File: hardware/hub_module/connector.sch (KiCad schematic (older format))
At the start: 4 parts, among them U2 conn2x18pcie

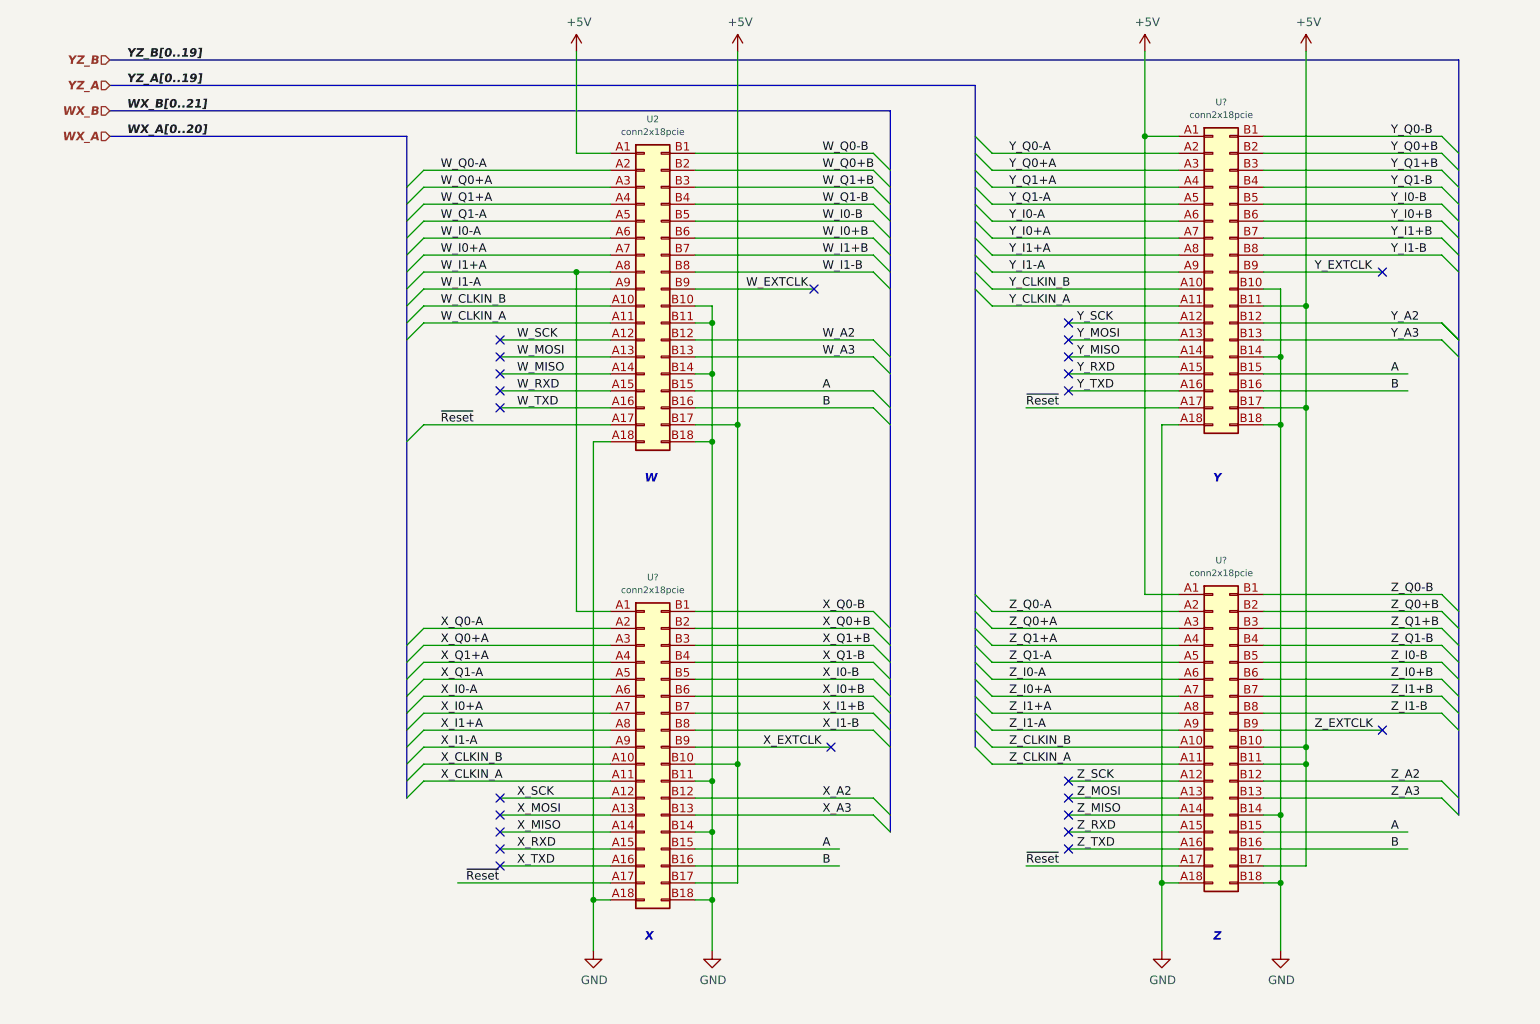
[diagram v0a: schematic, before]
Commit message: busses added
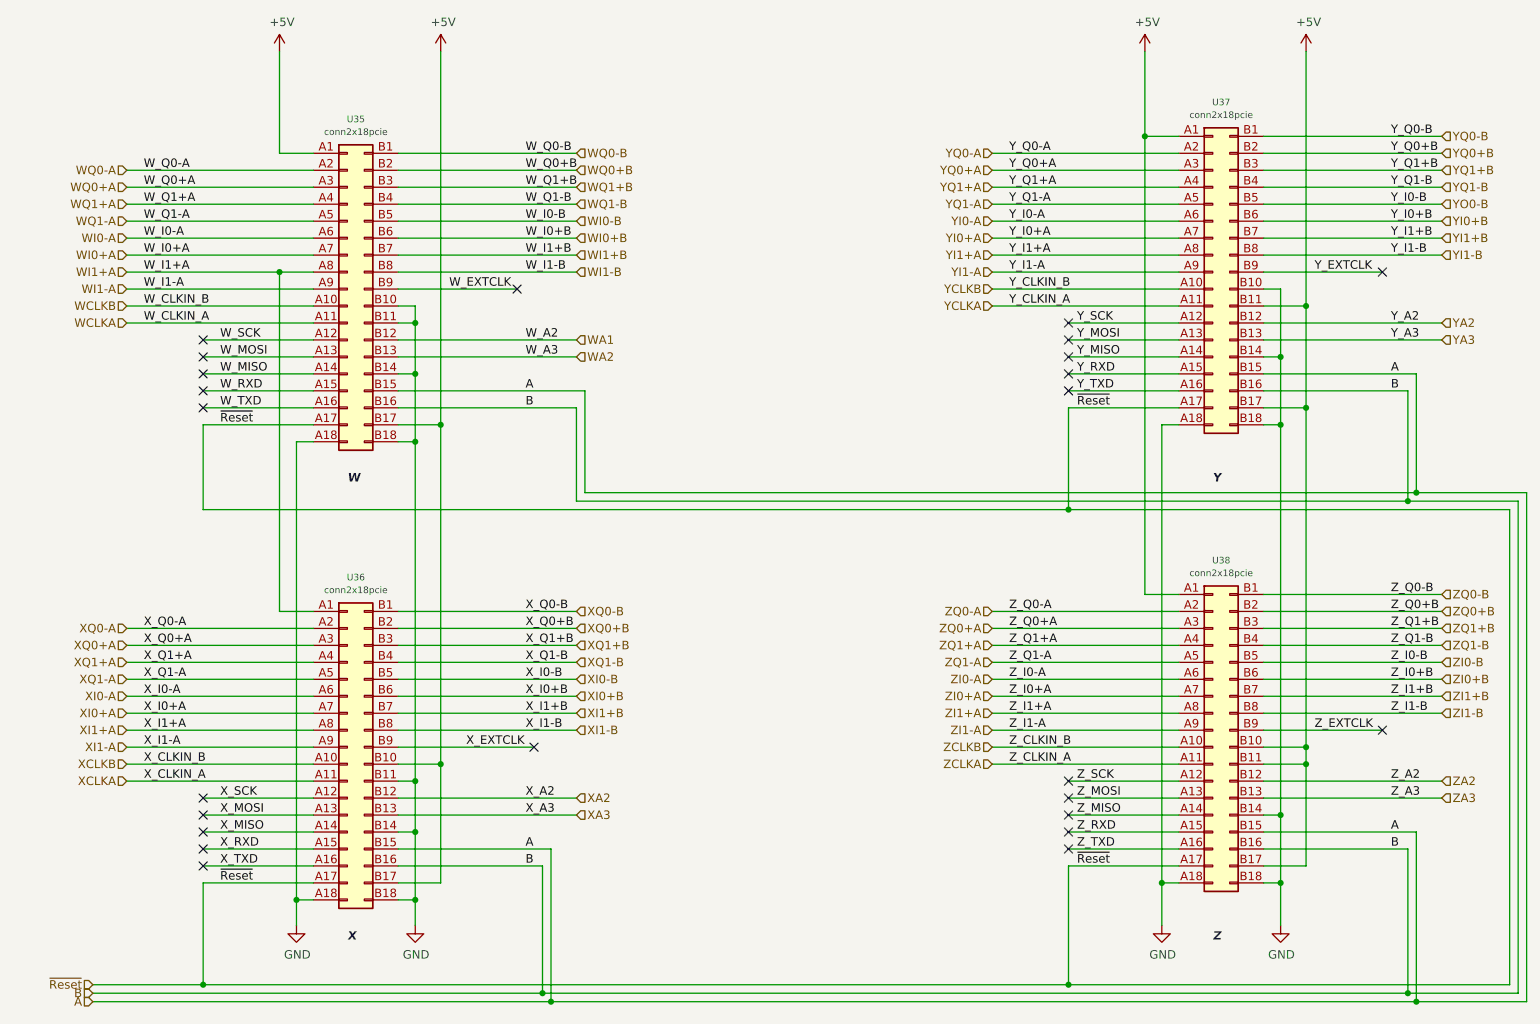
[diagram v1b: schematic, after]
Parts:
- gave numbers to parts that had none: 3
- renumbered U2 to U35
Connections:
- net labels added: WA1, WA2, WCLKA, WCLKB, WI0+A, WI0+B, WI0-A, WI0-B, WI1+A, WI1+B, WI1-A, WI1-B, WQ0+A, WQ0+B, WQ0-A, WQ0-B, WQ1+A, WQ1+B, WQ1-A, WQ1-B, XA2, XA3, XCLKA, XCLKB, XI0+A, XI0+B, XI0-A, XI0-B, XI1+A, XI1+B, XI1-A, XI1-B, XQ0+A, XQ0+B, XQ0-A, XQ0-B, XQ1+A, XQ1+B, XQ1-A, XQ1-B, YA2, YA3, YCLKA, YCLKB, YI0+A, YI0+B, YI0-A, YI1+A, YI1+B, YI1-A, YI1-B, YO0-B, YQ0+A, YQ0+B, YQ0-A, YQ0-B, YQ1+A, YQ1+B, YQ1-A, YQ1-B, ZA2, ZA3, ZCLKA, ZCLKB, ZI0+A, ZI0+B, ZI0-A, ZI0-B, ZI1+A, ZI1+B, ZI1-A, ZI1-B, ZQ0+A, ZQ0+B, ZQ0-A, ZQ0-B, ZQ1+A, ZQ1+B, ZQ1-A, ZQ1-B
- net labels removed: WX_A, WX_A[0..20], WX_B, WX_B[0..21], YZ_A, YZ_A[0..19], YZ_B, YZ_B[0..19]
- wire segments 173 -> 203
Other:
- moved on the sheet: U35, U36
